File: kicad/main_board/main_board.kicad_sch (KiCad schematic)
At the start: 8 parts

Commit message: add generation script
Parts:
- FID1, FID2, FID3, H1, H2, H3, H4, H5: Service (none) -> PCBA;HandAssembly
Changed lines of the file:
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@@
 			)
 		)
-		(property "JLC" ""
+		(property "Service" "PCBA;HandAssembly"
 			(at 96.52 189.23 0)
 			(effects
@@
 			)
 		)
-		(property "JLC" ""
+		(property "Service" "PCBA;HandAssembly"
 			(at 34.29 180.34 0)
 			(effects
@@
 			)
 		)
-		(property "JLC" ""
+		(property "Service" "PCBA;HandAssembly"
 			(at 48.26 180.34 0)
 			(effects
@@
 			)
 		)
-		(property "JLC" ""
+		(property "Service" "PCBA;HandAssembly"
 			(at 39.37 189.23 0)
 			(effects
@@
 			)
 		)
-		(property "JLC" ""
+		(property "Service" "PCBA;HandAssembly"
 			(at 20.32 189.23 0)
 			(effects
@@
 			)
 		)
-		(property "JLC" ""
+		(property "Service" "PCBA;HandAssembly"
 			(at 58.42 189.23 0)
 			(effects
@@
 			)
 		)
-		(property "JLC" ""
+		(property "Service" "PCBA;HandAssembly"
 			(at 77.47 189.23 0)
 			(effects
@@
 			)
 		)
-		(property "JLC" ""
+		(property "Service" "PCBA;HandAssembly"
 			(at 20.32 180.34 0)
 			(effects

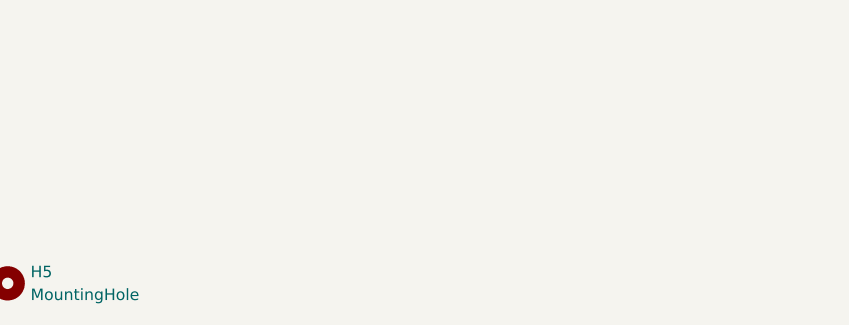
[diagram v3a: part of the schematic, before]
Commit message: add standoff holes for output board
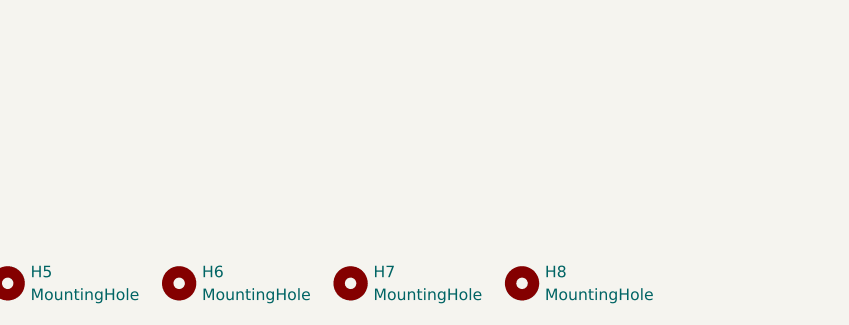
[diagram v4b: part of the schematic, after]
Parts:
- added H6, H7, H8: MountingHole, MountingHole:MountingHole_2.2mm_M2, symbol Mechanical:MountingHole
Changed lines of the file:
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@@
+	)
+	(symbol
+		(lib_id "Mechanical:MountingHole")
+		(at 153.67 189.23 0)
+		(unit 1)
+		(exclude_from_sim yes)
+		(in_bom no)
+		(on_board yes)
+		(dnp no)
+		(fields_autoplaced yes)
+		(property "Reference" "H8"
+			(at 156.21 187.9599 0)
+			(effects
+				(font
+					(size 1.27 1.27)
+				)
+				(justify left)
+			)
+		)
+		(property "Value" "MountingHole"
+			(at 156.21 190.4999 0)
+			(effects
+				(font
+					(size 1.27 1.27)
+				)
+				(justify left)
+			)
+		)
+		(property "Footprint" "MountingHole:MountingHole_2.2mm_M2"
+			(at 153.67 189.23 0)
+			(effects
+				(font
+					(size 1.27 1.27)
+				)
+				(hide yes)
+			)
+		)
+		(property "Datasheet" "~"
+			(at 153.67 189.23 0)
+			(effects
+				(font
+					(size 1.27 1.27)
+				)
+				(hide yes)
+			)
+		)
+		(property "Description" "Mounting Hole without connection"
+			(at 153.67 189.23 0)
+			(effects
+				(font
+					(size 1.27 1.27)
+				)
+				(hide yes)
+			)
+		)
+		(property "Service" "PCBA;HandAssembly"
+			(at 153.67 189.23 0)
+			(effects
+				(font
+					(size 1.27 1.27)
+				)
+				(hide yes)
+			)
+		)
+		(instances
+			(project "main_board"
+				(path "/8e1f1504-76c2-49e6-9261-3c1190503f8c"
+					(reference "H8")
+					(unit 1)
+				)
+			)
+		)
 	)
 	(symbol
@@
 	(symbol
 		(lib_id "Mechanical:MountingHole")
+		(at 134.62 189.23 0)
+		(unit 1)
+		(exclude_from_sim yes)
+		(in_bom no)
+		(on_board yes)
+		(dnp no)
+		(fields_autoplaced yes)
+		(property "Reference" "H7"
+			(at 137.16 187.9599 0)
+			(effects
+				(font
+					(size 1.27 1.27)
+				)
+				(justify left)
+			)
+		)
+		(property "Value" "MountingHole"
+			(at 137.16 190.4999 0)
+			(effects
+				(font
+					(size 1.27 1.27)
+				)
+				(justify left)
+			)
+		)
+		(property "Footprint" "MountingHole:MountingHole_2.2mm_M2"
+			(at 134.62 189.23 0)
+			(effects
+				(font
+					(size 1.27 1.27)
+				)
+				(hide yes)
+			)
+		)
+		(property "Datasheet" "~"
+			(at 134.62 189.23 0)
+			(effects
+				(font
+					(size 1.27 1.27)
+				)
+				(hide yes)
+			)
+		)
+		(property "Description" "Mounting Hole without connection"
+			(at 134.62 189.23 0)
+			(effects
+				(font
+					(size 1.27 1.27)
+				)
+				(hide yes)
+			)
+		)
+		(property "Service" "PCBA;HandAssembly"
+			(at 134.62 189.23 0)
+			(effects
+				(font
+					(size 1.27 1.27)
+				)
+				(hide yes)
+			)
+		)
+		(instances
+			(project "main_board"
+				(path "/8e1f1504-76c2-49e6-9261-3c1190503f8c"
+					(reference "H7")
+					(unit 1)
+				)
+			)
+		)
+	)
+	(symbol
+		(lib_id "Mechanical:MountingHole")
 		(at 20.32 189.23 0)
 		(unit 1)
@@
 					(unit 1)
 				)
+			)
+		)
+	)
+	(symbol
+		(lib_id "Mechanical:MountingHole")
+		(at 115.57 189.23 0)
+		(unit 1)
+		(exclude_from_sim yes)
+		(in_bom no)
+		(on_board yes)
+		(dnp no)
+		(fields_autoplaced yes)
+		(property "Reference" "H6"
+			(at 118.11 187.9599 0)
+			(effects
+				(font
+					(size 1.27 1.27)
+				)
+				(justify left)
+			)
+		)
+		(property "Value" "MountingHole"
+			(at 118.11 190.4999 0)
+			(effects
+				(font
+					(size 1.27 1.27)
+				)
+				(justify left)
+			)
+		)
+		(property "Footprint" "MountingHole:MountingHole_2.2mm_M2"
+			(at 115.57 189.23 0)
+			(effects
+				(font
+					(size 1.27 1.27)
+				)
+				(hide yes)
+			)
+		)
+		(property "Datasheet" "~"
+			(at 115.57 189.23 0)
+			(effects
+				(font
+					(size 1.27 1.27)
+				)
+				(hide yes)
+			)
+		)
+		(property "Description" "Mounting Hole without connection"
+			(at 115.57 189.23 0)
+			(effects
+				(font
+					(size 1.27 1.27)
+				)
+				(hide yes)
+			)
+		)
+		(property "Service" "PCBA;HandAssembly"
+			(at 115.57 189.23 0)
+			(effects
+				(font
+					(size 1.27 1.27)
+				)
+				(hide yes)
+			)
+		)
+		(instances
+			(project "main_board"
+				(path "/8e1f1504-76c2-49e6-9261-3c1190503f8c"
+					(reference "H6")
+					(unit 1)
+				)

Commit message: fix title block
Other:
- title: SW32 - Main Board -> SW32
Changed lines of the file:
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@@
 	(paper "A4")
 	(title_block
-		(title "SW32 - Main Board")
-		(date "2024-06-11")
+		(title "SW32")
+		(date "2024-06-12")
 		(rev "1")
 		(company "saawsm")
